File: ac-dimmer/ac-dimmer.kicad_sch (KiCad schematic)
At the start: 74 parts, among them J1 Screw_Terminal_01x02, J2 Screw_Terminal_01x02, J3 Conn_01x06_Pin, J4 Screw_Terminal_01x02, J6 Screw_Terminal_01x02, J7 Screw_Terminal_01x02, Q1 IRF840, Q10 KSP44, Q11 IRF840, Q12 IRF840, Q13 KSP44, Q14 IRF840, Q15 IRF840, Q2 KSP44, Q3 KSP44, Q4 IRF840, Q5 IRF840, Q6 IRF840, U1 FL5150MX, U2 MCP4451, U3 FL5150MX, U5 FL5150MX, U6 FL5150MX

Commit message: Dimmer: Assign footprints
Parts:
- C1: renamed from C15; footprint (none) -> Capacitor_SMD:C_1206_3216Metric
- C10: renamed from C11; footprint (none) -> Capacitor_SMD:C_1206_3216Metric
- C11: renamed from C8; footprint (none) -> Capacitor_SMD:C_1206_3216Metric
- C12: renamed from C10; footprint (none) -> Capacitor_SMD:C_1206_3216Metric
- C13: renamed from C6; footprint (none) -> Capacitor_SMD:C_1206_3216Metric
- C14: renamed from C3; footprint (none) -> Capacitor_SMD:C_1206_3216Metric
- C15: renamed from C7; footprint (none) -> Capacitor_SMD:C_1206_3216Metric
- C16: renamed from C12; footprint (none) -> Capacitor_SMD:C_1206_3216Metric
- C17: renamed from C13; footprint (none) -> Capacitor_SMD:C_1206_3216Metric
- C2: renamed from C16; footprint (none) -> Capacitor_SMD:C_1206_3216Metric
- C3: renamed from C1; footprint (none) -> Capacitor_SMD:C_1206_3216Metric
- C4: renamed from C5; footprint (none) -> Capacitor_SMD:C_1206_3216Metric
- C5: renamed from C2; footprint (none) -> Capacitor_SMD:C_1206_3216Metric
- C6: renamed from C4; footprint (none) -> Capacitor_SMD:C_1206_3216Metric
- C7: renamed from C14; footprint (none) -> Capacitor_SMD:C_1206_3216Metric
- C8: renamed from C17; footprint (none) -> Capacitor_SMD:C_1206_3216Metric
- C9: footprint (none) -> Capacitor_SMD:C_1206_3216Metric
- D1, D2: footprint (none) -> Diode_THT:D_DO-41_SOD81_P10.16mm_Horizontal
- D3: renamed from D4; footprint (none) -> Diode_THT:D_DO-41_SOD81_P10.16mm_Horizontal
- D4: renamed from D5; footprint (none) -> Diode_THT:D_DO-41_SOD81_P10.16mm_Horizontal
- J1: footprint (none) -> TerminalBlock_Phoenix:TerminalBlock_Phoenix_MKDS-1,5-2-5.08_1x02_P5.08mm_Horizontal
- J2: renamed from J4; footprint (none) -> TerminalBlock_Phoenix:TerminalBlock_Phoenix_MKDS-1,5-2-5.08_1x02_P5.08mm_Horizontal
- J3: renamed from J6; footprint (none) -> TerminalBlock_Phoenix:TerminalBlock_Phoenix_MKDS-1,5-2-5.08_1x02_P5.08mm_Horizontal
- J4: renamed from J7; footprint (none) -> TerminalBlock_Phoenix:TerminalBlock_Phoenix_MKDS-1,5-2-5.08_1x02_P5.08mm_Horizontal
- J5: renamed from J3; footprint (none) -> Connector_PinHeader_2.54mm:PinHeader_1x06_P2.54mm_Vertical
- J6: renamed from J2; footprint (none) -> TerminalBlock_Phoenix:TerminalBlock_Phoenix_MKDS-1,5-2-5.08_1x02_P5.08mm_Horizontal
- JP1: footprint (none) -> Connector_PinHeader_2.54mm:PinHeader_1x03_P2.54mm_Vertical
- JP2: renamed from JP4; footprint (none) -> Connector_PinHeader_2.54mm:PinHeader_1x03_P2.54mm_Vertical
- JP3: renamed from JP6; footprint (none) -> Connector_PinHeader_2.54mm:PinHeader_1x03_P2.54mm_Vertical
- JP4: renamed from JP7; footprint (none) -> Connector_PinHeader_2.54mm:PinHeader_1x03_P2.54mm_Vertical
- JP5: renamed from JP2; footprint (none) -> Jumper:SolderJumper-3_P1.3mm_Open_Pad1.0x1.5mm
- JP6: renamed from JP3; footprint (none) -> Jumper:SolderJumper-3_P1.3mm_Open_Pad1.0x1.5mm
- Q1: footprint (none) -> Package_TO_SOT_THT:TO-220-3_Vertical
- Q10: renamed from Q15; footprint (none) -> Package_TO_SOT_THT:TO-220-3_Vertical
- Q11: renamed from Q10; footprint (none) -> Package_TO_SOT_THT:TO-92_Inline
- Q12: renamed from Q13; footprint (none) -> Package_TO_SOT_THT:TO-92_Inline
- Q2: renamed from Q5; footprint (none) -> Package_TO_SOT_THT:TO-220-3_Vertical
- Q3: renamed from Q4; footprint (none) -> Package_TO_SOT_THT:TO-220-3_Vertical
- Q4: renamed from Q6; footprint (none) -> Package_TO_SOT_THT:TO-220-3_Vertical
- Q5: renamed from Q3; footprint (none) -> Package_TO_SOT_THT:TO-92_Inline
- Q6: renamed from Q2; footprint (none) -> Package_TO_SOT_THT:TO-92_Inline
- Q7: renamed from Q11; footprint (none) -> Package_TO_SOT_THT:TO-220-3_Vertical
- Q8: renamed from Q14; footprint (none) -> Package_TO_SOT_THT:TO-220-3_Vertical
- Q9: renamed from Q12; footprint (none) -> Package_TO_SOT_THT:TO-220-3_Vertical
- R1, R12: footprint (none) -> Package_TO_SOT_THT:TO-92L_Wide
- R10: renamed from R11; footprint (none) -> Package_TO_SOT_THT:TO-92L_Wide
- R11: renamed from R5; footprint (none) -> Package_TO_SOT_THT:TO-92L_Wide
- R13: renamed from R20; footprint (none) -> Package_TO_SOT_THT:TO-92L_Wide
- R14: renamed from R26; footprint (none) -> Package_TO_SOT_THT:TO-92L_Wide
- R15: renamed from R19; footprint (none) -> Package_TO_SOT_THT:TO-92L_Wide
- R16: renamed from R25; footprint (none) -> Package_TO_SOT_THT:TO-92L_Wide
- R17: renamed from R21; footprint (none) -> Package_TO_SOT_THT:TO-92L_Wide
- R18: renamed from R27; footprint (none) -> Package_TO_SOT_THT:TO-92L_Wide
- R19: renamed from R22; footprint (none) -> Package_TO_SOT_THT:TO-92L_Wide
- R2: renamed from R8; footprint (none) -> Package_TO_SOT_THT:TO-92L_Wide
- R20: renamed from R28; footprint (none) -> Package_TO_SOT_THT:TO-92L_Wide
- R21: renamed from R23; footprint (none) -> Package_TO_SOT_THT:TO-92L_Wide
- R22: renamed from R29; footprint (none) -> Package_TO_SOT_THT:TO-92L_Wide
- R23: renamed from R24; footprint (none) -> Package_TO_SOT_THT:TO-92L_Wide
- R24: renamed from R30; footprint (none) -> Package_TO_SOT_THT:TO-92L_Wide
- R3: renamed from R6; footprint (none) -> Package_TO_SOT_THT:TO-92L_Wide
- R4: renamed from R7; footprint (none) -> Package_TO_SOT_THT:TO-92L_Wide
- R5: renamed from R2; footprint (none) -> Package_TO_SOT_THT:TO-92L_Wide
- R6: renamed from R9; footprint (none) -> Package_TO_SOT_THT:TO-92L_Wide
- R7: renamed from R3; footprint (none) -> Package_TO_SOT_THT:TO-92L_Wide
- R8: renamed from R10; footprint (none) -> Package_TO_SOT_THT:TO-92L_Wide
- R9: renamed from R4; footprint (none) -> Package_TO_SOT_THT:TO-92L_Wide
- renumbered U3 to U2, U5 to U3, U6 to U4, U2 to U5

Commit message: [WIP] Layout AC dimmer
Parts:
- R1, R10, R11, R12, R13, R14, R15, R16, R17, R18, R19, R2, R20, R21, R22, R23, R24, R3, R4, R5, R6, R7, R8, R9: footprint Package_TO_SOT_THT:TO-92L_Wide -> Resistor_SMD:R_1206_3216Metric
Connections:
- net LP_DIM_1: now reaches Q5.2 (B), R9.1, U1.7 (Low_Power)
- net A1: now reaches JP6.2 (C), U5.16 (A1)
- net GATE_DIM_1: now reaches C3.1, Q1.1 (G), Q3.1 (G), R5.2
- net VS_DIM_1: now reaches C5.1, Q5.1 (E), U1.6 (VS)
- net MODE_DIM_1: now reaches JP1.2 (C), U1.4 (DIM_Mode)
- net A0: now reaches JP5.2 (C), U5.4 (HVC/A0)
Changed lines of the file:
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@@
     (effects (font (size 4 4)) (justify left bottom))
   )
+  (label "A0" (at 41.91 356.87 0) (fields_autoplaced)
+    (effects (font (size 1.27 1.27)) (justify left bottom))
+  )
+  (label "MODE_DIM_1" (at 60.96 82.55 180) (fields_autoplaced)
+    (effects (font (size 1.27 1.27)) (justify right bottom))
+  )
+  (label "LP_DIM_1" (at 111.76 85.09 180) (fields_autoplaced)
+    (effects (font (size 1.27 1.27)) (justify right bottom))
+  )
+  (label "A1" (at 55.88 374.65 0) (fields_autoplaced)
+    (effects (font (size 1.27 1.27)) (justify left bottom))
+  )
+  (label "GATE_DIM_1" (at 130.81 69.85 0) (fields_autoplaced)
+    (effects (font (size 1.27 1.27)) (justify left bottom))
+  )
+  (label "VS_DIM_1" (at 95.25 90.17 180) (fields_autoplaced)
+    (effects (font (size 1.27 1.27)) (justify right bottom))
+  )
   (global_label "MAINS_LIVE_OUT_4" (shape input) (at 355.6 212.09 0) (fields_autoplaced)
     (effects (font (size 1.27 1.27)) (justify left))
@@
       (effects (font (size 1.27 1.27)))
     )
-    (property "Footprint" "Package_TO_SOT_THT:TO-92L_Wide" (at 120.65 86.868 90)
+    (property "Footprint" "Resistor_SMD:R_1206_3216Metric" (at 120.65 86.868 90)
       (effects (font (size 1.27 1.27)) hide)
     )
@@
       (effects (font (size 1.27 1.27)))
     )
-    (property "Footprint" "Package_TO_SOT_THT:TO-92L_Wide" (at 311.15 188.468 90)
+    (property "Footprint" "Resistor_SMD:R_1206_3216Metric" (at 311.15 188.468 90)
       (effects (font (size 1.27 1.27)) hide)
     )
@@
       (effects (font (size 1.27 1.27)))
     )
-    (property "Footprint" "Package_TO_SOT_THT:TO-92L_Wide" (at 311.15 79.248 90)
+    (property "Footprint" "Resistor_SMD:R_1206_3216Metric" (at 311.15 79.248 90)
       (effects (font (size 1.27 1.27)) hide)
     )
@@
       (effects (font (size 1.27 1.27)))
     )
-    (property "Footprint" "Package_TO_SOT_THT:TO-92L_Wide" (at 245.11 193.548 90)
+    (property "Footprint" "Resistor_SMD:R_1206_3216Metric" (at 245.11 193.548 90)
       (effects (font (size 1.27 1.27)) hide)
     )
@@
       (effects (font (size 1.27 1.27)))
     )
-    (property "Footprint" "Package_TO_SOT_THT:TO-92L_Wide" (at 120.65 211.328 90)
+    (property "Footprint" "Resistor_SMD:R_1206_3216Metric" (at 120.65 211.328 90)
       (effects (font (size 1.27 1.27)) hide)
     )
@@
       (effects (font (size 1.27 1.27)))
     )
-    (property "Footprint" "Package_TO_SOT_THT:TO-92L_Wide" (at 120.65 71.628 90)
+    (property "Footprint" "Resistor_SMD:R_1206_3216Metric" (at 120.65 71.628 90)
       (effects (font (size 1.27 1.27)) hide)
     )
@@
       (effects (font (size 1.27 1.27)))
     )
-    (property "Footprint" "Package_TO_SOT_THT:TO-92L_Wide" (at 311.15 203.708 90)
+    (property "Footprint" "Resistor_SMD:R_1206_3216Metric" (at 311.15 203.708 90)
       (effects (font (size 1.27 1.27)) hide)
     )
@@
       (effects (font (size 1.27 1.27)))
     )
-    (property "Footprint" "Package_TO_SOT_THT:TO-92L_Wide" (at 120.65 79.248 90)
+    (property "Footprint" "Resistor_SMD:R_1206_3216Metric" (at 120.65 79.248 90)
       (effects (font (size 1.27 1.27)) hide)
     )
@@
       (effects (font (size 1.27 1.27)))
     )
-    (property "Footprint" "Package_TO_SOT_THT:TO-92L_Wide" (at 311.15 211.328 90)
+    (property "Footprint" "Resistor_SMD:R_1206_3216Metric" (at 311.15 211.328 90)
       (effects (font (size 1.27 1.27)) hide)
     )
@@
       (effects (font (size 1.27 1.27)))
     )
-    (property "Footprint" "Package_TO_SOT_THT:TO-92L_Wide" (at 54.61 193.548 90)
+    (property "Footprint" "Resistor_SMD:R_1206_3216Metric" (at 54.61 193.548 90)
       (effects (font (size 1.27 1.27)) hide)
     )
@@
       (effects (font (size 1.27 1.27)))
     )
-    (property "Footprint" "Package_TO_SOT_THT:TO-92L_Wide" (at 120.65 196.088 90)
+    (property "Footprint" "Resistor_SMD:R_1206_3216Metric" (at 120.65 196.088 90)
       (effects (font (size 1.27 1.27)) hide)
     )
@@
       (effects (font (size 1.27 1.27)))
     )
-    (property "Footprint" "Package_TO_SOT_THT:TO-92L_Wide" (at 311.15 86.868 90)
+    (property "Footprint" "Resistor_SMD:R_1206_3216Metric" (at 311.15 86.868 90)
       (effects (font (size 1.27 1.27)) hide)
     )
@@
       (effects (font (size 1.27 1.27)))
     )
-    (property "Footprint" "Package_TO_SOT_THT:TO-92L_Wide" (at 311.15 94.488 90)
+    (property "Footprint" "Resistor_SMD:R_1206_3216Metric" (at 311.15 94.488 90)
       (effects (font (size 1.27 1.27)) hide)
     )
@@
       (effects (font (size 1.27 1.27)))
     )
-    (property "Footprint" "Package_TO_SOT_THT:TO-92L_Wide" (at 311.15 196.088 90)
+    (property "Footprint" "Resistor_SMD:R_1206_3216Metric" (at 311.15 196.088 90)
       (effects (font (size 1.27 1.27)) hide)
     )
@@
       (effects (font (size 1.27 1.27)))
     )
-    (property "Footprint" "Package_TO_SOT_THT:TO-92L_Wide" (at 245.11 69.088 90)
+    (property "Footprint" "Resistor_SMD:R_1206_3216Metric" (at 245.11 69.088 90)
       (effects (font (size 1.27 1.27)) hide)
     )
@@
       (effects (font (size 1.27 1.27)))
     )
-    (property "Footprint" "Package_TO_SOT_THT:TO-92L_Wide" (at 54.61 69.088 90)
+    (property "Footprint" "Resistor_SMD:R_1206_3216Metric" (at 54.61 69.088 90)
       (effects (font (size 1.27 1.27)) hide)
     )
@@
       (effects (font (size 1.27 1.27)))
     )
-    (property "Footprint" "Package_TO_SOT_THT:TO-92L_Wide" (at 311.15 64.008 90)
+    (property "Footprint" "Resistor_SMD:R_1206_3216Metric" (at 311.15 64.008 90)
       (effects (font (size 1.27 1.27)) hide)
     )
@@
       (effects (font (size 1.27 1.27)))
     )
-    (property "Footprint" "Package_TO_SOT_THT:TO-92L_Wide" (at 120.65 218.948 90)
+    (property "Footprint" "Resistor_SMD:R_1206_3216Metric" (at 120.65 218.948 90)
       (effects (font (size 1.27 1.27)) hide)
     )
@@
       (effects (font (size 1.27 1.27)))
     )
-    (property "Footprint" "Package_TO_SOT_THT:TO-92L_Wide" (at 311.15 71.628 90)
+    (property "Footprint" "Resistor_SMD:R_1206_3216Metric" (at 311.15 71.628 90)
       (effects (font (size 1.27 1.27)) hide)
     )
@@
       (effects (font (size 1.27 1.27)))
     )
-    (property "Footprint" "Package_TO_SOT_THT:TO-92L_Wide" (at 120.65 188.468 90)
+    (property "Footprint" "Resistor_SMD:R_1206_3216Metric" (at 120.65 188.468 90)
       (effects (font (size 1.27 1.27)) hide)
     )
@@
       (effects (font (size 1.27 1.27)))
     )
-    (property "Footprint" "Package_TO_SOT_THT:TO-92L_Wide" (at 311.15 218.948 90)
+    (property "Footprint" "Resistor_SMD:R_1206_3216Metric" (at 311.15 218.948 90)
       (effects (font (size 1.27 1.27)) hide)
     )
@@
       (effects (font (size 1.27 1.27)))
     )
-    (property "Footprint" "Package_TO_SOT_THT:TO-92L_Wide" (at 120.65 64.008 90)
+    (property "Footprint" "Resistor_SMD:R_1206_3216Metric" (at 120.65 64.008 90)
       (effects (font (size 1.27 1.27)) hide)
     )
@@
       (effects (font (size 1.27 1.27)))
     )
-    (property "Footprint" "Package_TO_SOT_THT:TO-92L_Wide" (at 120.65 94.488 90)
+    (property "Footprint" "Resistor_SMD:R_1206_3216Metric" (at 120.65 94.488 90)
       (effects (font (size 1.27 1.27)) hide)
     )
@@
       (effects (font (size 1.27 1.27)))
     )
-    (property "Footprint" "Package_TO_SOT_THT:TO-92L_Wide" (at 120.65 203.708 90)
+    (property "Footprint" "Resistor_SMD:R_1206_3216Metric" (at 120.65 203.708 90)
       (effects (font (size 1.27 1.27)) hide)
     )

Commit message: Finish AC dimmer layout and add production files
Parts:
- removed C10, C9: 22nF, Capacitor_SMD:C_1206_3216Metric, symbol Device:C
- removed C11, C12, C6: 4.7uF, Capacitor_SMD:C_1206_3216Metric, symbol Device:C
- removed C13, C14, C15, C16, C17, C7, C8: 0.1uF, Capacitor_SMD:C_1206_3216Metric, symbol Device:C
- removed D2, D3, D4: 1N4007, Diode_THT:D_DO-41_SOD81_P10.16mm_Horizontal, symbol Device:D
- removed J3, J4: Screw_Terminal_01x02, TerminalBlock_Phoenix:TerminalBlock_Phoenix_MKDS-1,5-2-5.08_1x02_P5.08mm_Horizontal, symbol Connector:Screw_Terminal_01x02
- removed J5: Conn_01x06_Pin, Connector_PinHeader_2.54mm:PinHeader_1x06_P2.54mm_Vertical, symbol Connector:Conn_01x06_Pin
- removed JP2, JP3, JP4: Jumper_3_Open, Connector_PinHeader_2.54mm:PinHeader_1x03_P2.54mm_Vertical, symbol Jumper:Jumper_3_Open
- removed JP5, JP6: SolderJumper_3_Open, Jumper:SolderJumper-3_P1.3mm_Open_Pad1.0x1.5mm, symbol Jumper:SolderJumper_3_Open
- removed Q10, Q2, Q4, Q7, Q8, Q9: IRF840, Package_TO_SOT_THT:TO-220-3_Vertical, symbol Device:Q_NMOS_GDS
- removed Q11, Q12, Q6: KSP44, Package_TO_SOT_THT:TO-92_Inline, symbol Device:Q_NPN_EBC
- removed R14, R15, R16, R19, R20: 2MR, Resistor_SMD:R_1206_3216Metric, symbol Device:R
- removed R17, R18: 1kR, Resistor_SMD:R_1206_3216Metric, symbol Device:R
- removed R21, R22: 330kR, Resistor_SMD:R_1206_3216Metric, symbol Device:R
- removed R23, R24: 33kR, Resistor_SMD:R_1206_3216Metric, symbol Device:R
- removed U2, U3, U4: FL5150MX, Package_SO:SSOP-10_3.9x4.9mm_P1.00mm, symbol Driver_FET:FL5150MX
- removed U5: MCP4451, Package_SO:TSSOP-20_4.4x6.5mm_P0.65mm, symbol Potentiometer_Digital:MCP4451-xxxx-ST
- added H1, H2, H3, H4: MountingHole, MountingHole:MountingHole_2.7mm_M2.5_ISO7380, symbol Mechanical:MountingHole
- added J3: Conn_01x02_Pin, Connector_PinHeader_2.54mm:PinHeader_1x02_P2.54mm_Vertical, symbol Connector:Conn_01x02_Pin
- C3, C4: value 22nF -> 10nF
- R1, R2, R3, R4, R7: value 2MR -> 1MR
- R10: value 330kR -> 10k
- R11: value 33kR -> 10k
- R12: value 33kR -> 100k
- R13: value 2MR -> 100k
- R6: value 1kR -> 1MR
- R8: value 2MR -> 10k
- R9: value 330kR -> 100k
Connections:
- net GND_DIM_2 is gone; now on net GND: C2.2, C4.2
- net VDD_DIM_2 is gone; now on net DIM_CTRL: C2.1
- net LP_DIM_1: now also R13.1; no longer R9.1
- net MAINS_LIVE_IN: now also J2.1 (Pin_1); no longer R1.2, R13.2
- net MAINS_NEUTRAL: now also R6.1; no longer R3.1, R4.1
- net MAINS_NEUTRAL_CAT: now reaches D1.1 (K), R11.2, R9.2
- net at R8.1: now also R10.2
- net at R6.2: now also R3.1; no longer C4.1
- net at Q5.3 (C): now also R10.1; no longer R11.1
- net at R12.2: now also R9.1; no longer R10.2
- net at R12.1: now also R13.2
- net MAINS_LIVE_OUT: now reaches R4.2
- net MAINS_LIVE_OUT: now also J1.1 (Pin_1), Q3.2 (D)
- net at R2.1: now also R1.2
- net DIM_CTRL_1 renamed DIM_CTRL
- net DIM_CTRL: now also J3.1 (Pin_1)
- net GATE_DIM_1 renamed GATE
- net GATE: now also C4.1
- net GND_DIM_1 renamed GND
- net GND: now also J3.2 (Pin_2)
- removed net MAINS_LIVE_OUT_1: J1.1 (Pin_1), Q3.2 (D), R7.2
- net MAINS_LIVE_OUT_2: no longer names the net of R8.2
- net MAINS_LIVE_OUT_2: now also R11.1; no longer J2.1 (Pin_1)
- net MODE_DIM_1 renamed DIM_MODE
- net VDD_DIM_1 renamed VDD
- net VS_DIM_1 renamed VS_DIM
- new net: R4.1, R7.2
- no-connect marks 1 -> 0
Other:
- note added: "AC Dimmer"
- note added: "Dim Control (via External Resistor)"
- note added: "Mains Dimmed Output"
- note added: "Mains Input"
- note added: "Mounting Holes"
- note removed: "AC Dimmer Channel 1"
- note removed: "AC Dimmer Channel 2"
- note removed: "AC Dimmer Channel 3"
- note removed: "AC Dimmer Channel 4"
- note removed: "Digital Potentiometer"
- note removed: "MCU Interface"
- note removed: "Mains Power Supply"
- moved on the sheet: D1, J1, J6, R3

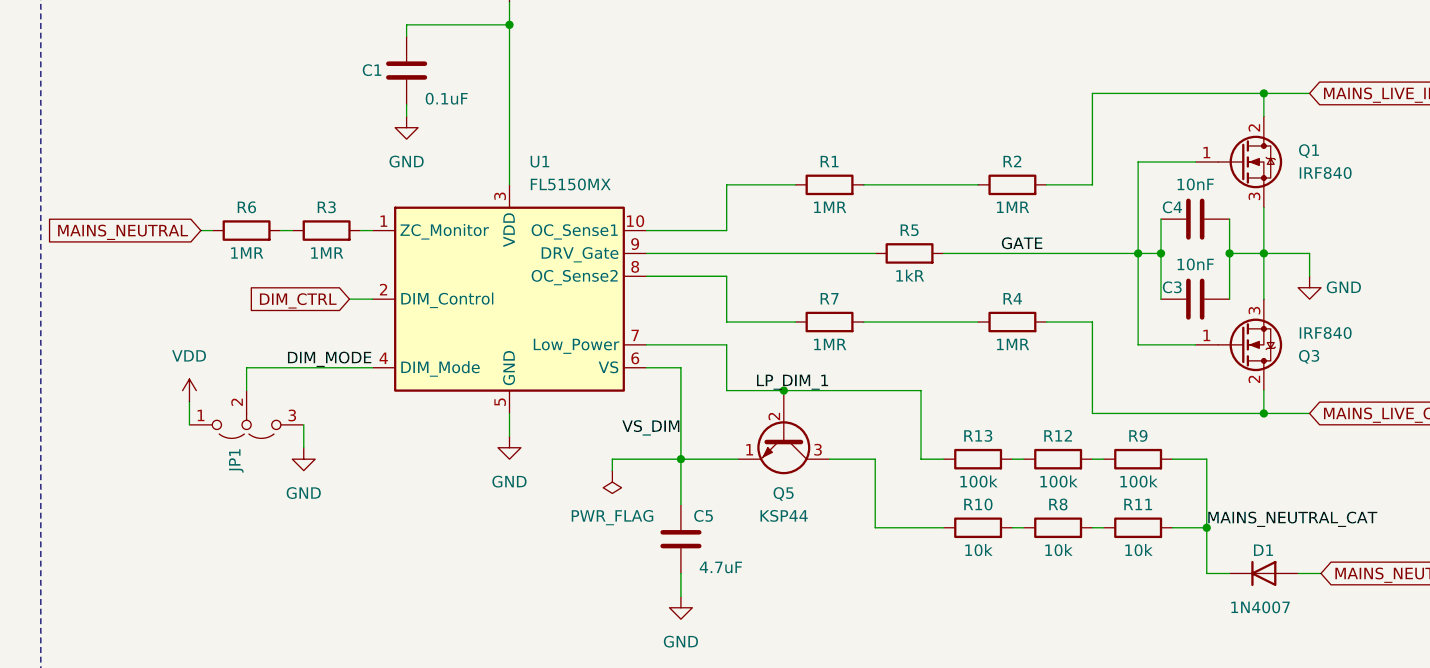
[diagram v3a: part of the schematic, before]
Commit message: Route 230V traces
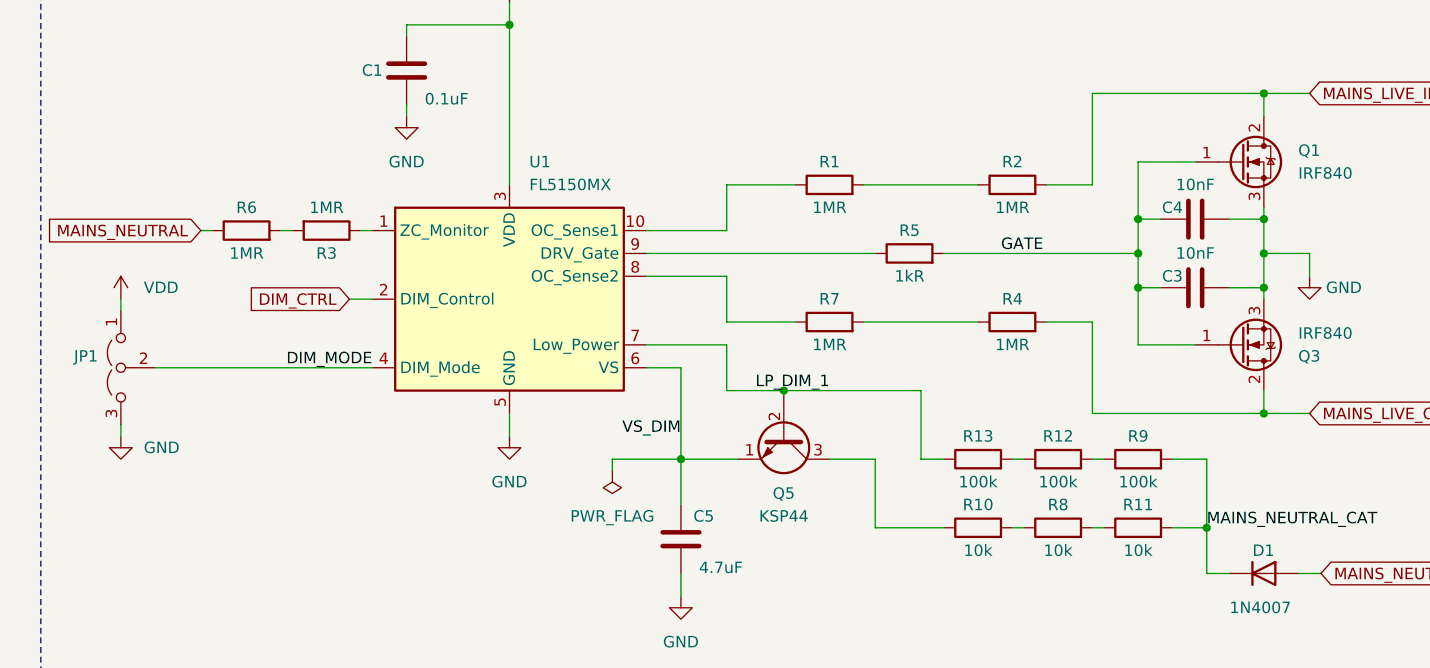
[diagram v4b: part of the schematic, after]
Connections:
- net at R3.1: now also U1.1 (ZC_Monitor); no longer R6.2
- net at R3.2: now also R6.2; no longer U1.1 (ZC_Monitor)
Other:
- moved on the sheet: C3, JP1, R3
